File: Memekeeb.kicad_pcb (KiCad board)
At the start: 2 copper layers, 117 parts, among them K1 KEYSW, K10 KEYSW, K11 KEYSW, K12 KEYSW, K14 KEYSW, K15 KEYSW, K16 KEYSW, K17 KEYSW, K18 KEYSW, K19 KEYSW, K2 KEYSW, K20 KEYSW, K21 KEYSW, K22 KEYSW, K23 KEYSW, K24 KEYSW, K25 KEYSW, K27 KEYSW, K28 KEYSW, K29 KEYSW, K3 KEYSW, K30 KEYSW, K31 KEYSW, K32 KEYSW, K33 KEYSW, K34 KEYSW, K35 KEYSW, K36 KEYSW, K37 KEYSW, K38 KEYSW, K4 KEYSW, K40 KEYSW, K41 KEYSW, K42 KEYSW, K43 KEYSW, K44 KEYSW, K45 KEYSW, K46 KEYSW, K47 KEYSW, K48 KEYSW, K49 KEYSW, K5 KEYSW, K50 KEYSW, K51 KEYSW, K6 KEYSW, K7 KEYSW, K8 KEYSW, K9 KEYSW, M2.6_1 VAL**, M2.6_2 VAL**, M2.6_3 VAL**, M2.6_4 VAL**, M2.6_5 VAL**, M2.6_6 VAL**, M2.6_7 VAL**

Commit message: Add unfinished pcb
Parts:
- removed    : LOGO, Graphics:Open-soos
- removed D26, D38, D39, D40, D41, D42, D43, D44, D45, D46, D47, D48, D49, D50, D51, D_ISOENTER1: D, keyboard_parts:D_SOD123_axial
- removed HOLE_M2.6_10, HOLE_M2.6_8, HOLE_M2.6_9, M2.6_1, M2.6_2, M2.6_3, M2.6_4, M2.6_5, M2.6_6, M2.6_7: VAL**, keyboard_parts:HOLE_M2.6
- removed K38, K40, K41, K42, K43, K44, K46, K47, K48, K49, K50, K51: KEYSW, Button_Switch_Keyboard:SW_Cherry_MX1A_1.00u_PCB
- removed K45: KEYSW, Button_Switch_Keyboard:SW_Cherry_MX1A_2.00u_PCB
- removed K_ENTER1, K_RSHFT1: KEYSW, Button_Switch_Keyboard:SW_Cherry_MX1A_1.50u_PCB
- added D_1.25u1: D, keyboard_parts:D_SOD123_axial, F.Cu at (169.1, 71.0)
- added D_2Uspc1: D, keyboard_parts:D_SOD123_axial, F.Cu at (169.1, 68.4)
- added K_1.25u1: KEYSW, Button_Switch_Keyboard:SW_Cherry_MX1A_1.25u_PCB, F.Cu at (148.0, 84.6)
- added K_2Uspc1: KEYSW, Keebio-Parts:MX-Alps-Choc-2U, F.Cu at (123.9, 109.8)
- added K_ENC1: Encoder_switch, Keebio-Parts:RotaryEncoder_Alps_EC11E-Switch_Vertical_H20mm, F.Cu at (276.7, 126.6)
- D1, D10, D11, D12, D13, D14, D15, D16, D17, D18, D19, D2, D20, D21, D22, D23, D24, D25, D27, D28, D29, D3, D30, D31, D32, D33, D34, D35, D36, D37, D4, D5, D6, D7, D8, D9: moved to F.Cu
- K1, K14, K27: footprint Button_Switch_Keyboard:SW_Cherry_MX1A_1.50u_PCB -> Keebio-Parts:MX-Alps-Choc-1U
- K10, K11, K12, K15, K16, K17, K18, K19, K2, K20, K21, K22, K23, K24, K25, K28, K29, K3, K30, K31, K32, K33, K34, K35, K36, K37, K4, K5, K6, K7, K8, K9: footprint Button_Switch_Keyboard:SW_Cherry_MX1A_1.00u_PCB -> Keebio-Parts:MX-Alps-Choc-1U
- K_BCKSPC1: footprint Button_Switch_Keyboard:SW_Cherry_MX1A_1.50u_PCB -> Keebio-Parts:MX_PCB_150H
- SW_RST1: value SW_RST -> SW_PUSH; moved to F.Cu
- moved K_BCKSPC1 220.2 mm to (119.0, 129.5)
- moved K_ISOENTER1 207.6 mm to (124.1, 76.0)
- moved D13 204.0 mm to (137.7, 159.7)
- moved D12 185.2 mm to (137.7, 162.3)
- moved K37 178.1 mm to (114.4, 148.5)
- moved D11 175.9 mm to (128.3, 159.7)
- moved D10 154.4 mm to (137.7, 164.9)
- moved K15 149.1 mm to (263.1, 90.7)
- moved D9 141.4 mm to (137.7, 167.5)
- moved D25 135.1 mm to (166.9, 105.8)
- moved K36 127.3 mm to (142.8, 129.6)
- moved D34 125.9 mm to (109.5, 159.4)
- moved D37 121.6 mm to (169.1, 73.6)
- moved D8 117.2 mm to (147.1, 162.3)
- moved D24 116.4 mm to (166.9, 108.4)
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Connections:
- net Net-(MCU_Pro_Micr0-Pad22) renamed RST
- net Net-(MCU_Pro_Micr0-Pad23) renamed GND
- K_ISOENTER1 pad 2: Net-(D_ISOENTER1-Pad2) -> RowB
- MCU_Pro_Micr0 pad 1: RowA -> Net-(MCU_Pro_Micr0-Pad1)
- MCU_Pro_Micr0 pad 10: ColD -> ColC
- MCU_Pro_Micr0 pad 11: ColE -> ColD
- MCU_Pro_Micr0 pad 12: ColF -> ColE
- MCU_Pro_Micr0 pad 13: Net-(MCU_Pro_Micr0-Pad13) -> ColM
- MCU_Pro_Micr0 pad 14: ColM -> ColL
- MCU_Pro_Micr0 pad 15: ColL -> ColK
- MCU_Pro_Micr0 pad 16: ColK -> ColJ
- MCU_Pro_Micr0 pad 17: ColJ -> ColI
- MCU_Pro_Micr0 pad 18: ColI -> ColH
- MCU_Pro_Micr0 pad 19: ColH -> ColG
- MCU_Pro_Micr0 pad 2: RowB -> Net-(MCU_Pro_Micr0-Pad2)
- MCU_Pro_Micr0 pad 20: ColG -> ColF
- MCU_Pro_Micr0 pad 5: RowC -> RowA
- MCU_Pro_Micr0 pad 6: RowD -> RowB
- MCU_Pro_Micr0 pad 7: ColA -> RowC
- MCU_Pro_Micr0 pad 8: ColB -> ColA
- MCU_Pro_Micr0 pad 9: ColC -> ColB
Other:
- board text removed: "> u/ergorius"

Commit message: Add WS2812B LED Strip support
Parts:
- removed D_2Uspc1: D, keyboard_parts:D_SOD123_axial
- added D_ISOENTR1: D, keyboard_parts:D_SOD123_axial, B.Cu at (283.8, 89.2)
- added LED_DATA1: 0, Keebio-Parts:SinglePad, B.Cu at (89.3, 95.3)
- added LED_GND1: 0, Keebio-Parts:SinglePad, B.Cu at (89.3, 98.6)
- added LED_PWR1: 0, Keebio-Parts:SinglePad, B.Cu at (89.5, 91.9)
- D1, D10, D11, D12, D13, D14, D15, D16, D17, D18, D19, D2, D20, D21, D22, D23, D24, D25, D27, D28, D29, D3, D30, D31, D32, D33, D34, D35, D36, D37, D4, D5, D6, D7, D8, D9, D_1.25u1, SW_RST1: moved to B.Cu
- K1, K10, K11, K12, K14, K15, K16, K17, K18, K19, K2, K20, K21, K22, K23, K24, K25, K27, K28, K29, K3, K30, K31, K32, K33, K34, K35, K36, K37, K4, K5, K6, K7, K8, K9: footprint Keebio-Parts:MX-Alps-Choc-1U -> Keebio-Parts:MX-Alps-Choc-1U-NoLED
- K_1.25u1: footprint Button_Switch_Keyboard:SW_Cherry_MX1A_1.25u_PCB -> Keebio-Parts:MX-Alps-Choc-1U-NoLED
- K_BCKSPC1: footprint Keebio-Parts:MX_PCB_150H -> Keebio-Parts:MX-Alps-Choc-1U-NoLED
- K_ISOENTER1: footprint Button_Switch_Keyboard:SW_Cherry_MX1A_ISOEnter_Plate -> Keebio-Parts:MX-Alps-Choc-2U
- moved K_ENC1 223.0 mm to (61.9, 66.7), turned to 90 degrees
- moved K_BCKSPC1 187.1 mm to (295.3, 66.7)
- moved K15 182.2 mm to (81.0, 85.7)
- moved D13 179.1 mm to (295.6, 75.2)
- moved K_ISOENTER1 174.7 mm to (297.7, 95.2), turned to 270 degrees
- moved D12 159.6 mm to (271.5, 75.3)
- moved D11 150.3 mm to (252.6, 75.2)
- moved K2 145.7 mm to (81.0, 66.7)
- moved K37 144.8 mm to (252.4, 104.8)
- moved K16 140.9 mm to (100.0, 85.7)
- moved K1 134.7 mm to (61.9, 66.7)
- moved D10 131.2 mm to (233.4, 75.2)
- moved K29 129.0 mm to (100.0, 104.8)
- moved K_1.25u1 127.5 mm to (273.9, 104.8)
- moved K4 124.9 mm to (119.1, 66.7)
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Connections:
- D11 pad 1: RowA -> RowD
- D12 pad 1: RowA -> RowD
- D13 pad 1: RowA -> RowD
- D24 pad 1: RowB -> RowD
- D25 pad 1: RowB -> RowD
- D37 pad 1: RowC -> RowD
- D_1.25u1 pad 1: RowC -> RowD
- K11 pad 1: ColK -> ColA
- K12 pad 1: ColL -> ColB
- K24 pad 1: ColK -> ColD
- K25 pad 1: ColL -> ColE
- K37 pad 1: ColK -> ColG
- K_1.25u1 pad 1: ColL -> ColH
- K_2Uspc1 pad 2: Net-(D_2Uspc1-Pad2) -> Net-(D32-Pad2)
- K_BCKSPC1 pad 1: ColM -> ColC
- K_ISOENTER1 pad 1: ColM -> ColF
- K_ISOENTER1 pad 2: RowB -> Net-(D_ISOENTR1-Pad2)
- MCU_Pro_Micr0 pad 1: Net-(MCU_Pro_Micr0-Pad1) -> EncA
- MCU_Pro_Micr0 pad 10: ColC -> RowD
- MCU_Pro_Micr0 pad 11: ColD -> ColA
- MCU_Pro_Micr0 pad 12: ColE -> ColB
- MCU_Pro_Micr0 pad 13: ColM -> ColJ
- MCU_Pro_Micr0 pad 14: ColL -> ColI
- MCU_Pro_Micr0 pad 15: ColK -> ColH
- MCU_Pro_Micr0 pad 16: ColJ -> ColG
- MCU_Pro_Micr0 pad 17: ColI -> ColF
- MCU_Pro_Micr0 pad 18: ColH -> ColC
- MCU_Pro_Micr0 pad 19: ColG -> ColD
- MCU_Pro_Micr0 pad 2: Net-(MCU_Pro_Micr0-Pad2) -> EncB
- MCU_Pro_Micr0 pad 20: ColF -> ColE
- MCU_Pro_Micr0 pad 21: Net-(MCU_Pro_Micr0-Pad21) -> RGB_PWR
- MCU_Pro_Micr0 pad 5: RowA -> RGB
- MCU_Pro_Micr0 pad 6: RowB -> Net-(MCU_Pro_Micr0-Pad6)
- MCU_Pro_Micr0 pad 7: RowC -> RowA
- MCU_Pro_Micr0 pad 8: ColA -> RowB
- MCU_Pro_Micr0 pad 9: ColB -> RowC

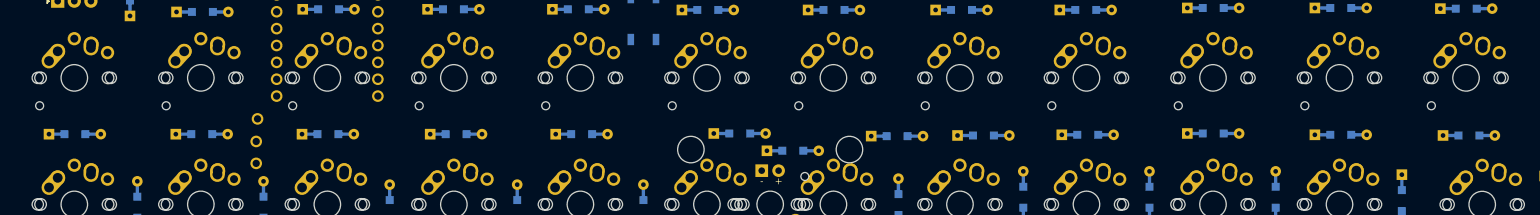
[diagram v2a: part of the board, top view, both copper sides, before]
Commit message: Move WS2812 pins to the side, rearrange diode footprints
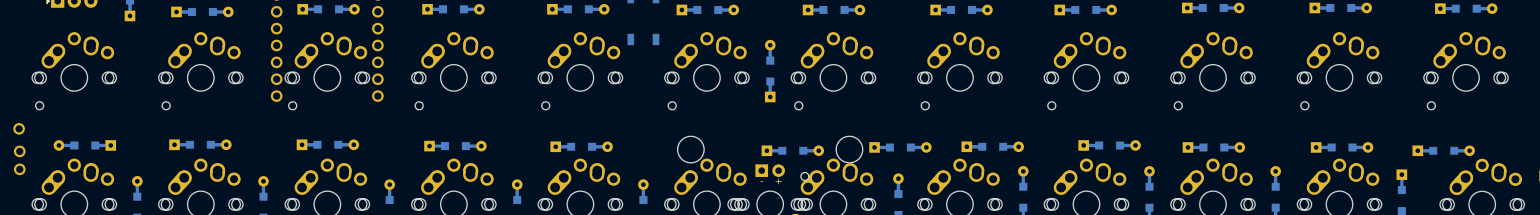
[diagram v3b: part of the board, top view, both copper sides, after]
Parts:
- LED_DATA1: value 0 -> DATA
- LED_GND1: value 0 -> GND
- LED_PWR1: value 0 -> PWR
- moved LED_PWR1 35.9 mm to (53.6, 93.4)
- moved LED_DATA1 35.6 mm to (53.7, 96.8)
- moved LED_GND1 35.6 mm to (53.7, 99.5)
- moved D19 10.5 mm to (166.7, 84.7), turned to 90 degrees
- moved D25 4.44 mm to (268.1, 96.7)
- moved D22 3.67 mm to (217.8, 95.9)
- moved D14 2.27 mm to (63.5, 95.9), turned to 180 degrees
- moved D21 2.20 mm to (200.2, 96.1)
- moved D23 2.10 mm to (233.5, 96.2)
- moved D24 1.91 mm to (252.8, 96.2)
- moved D18 1.90 mm to (138.3, 96.1)
- moved D17 1.80 mm to (119.3, 96.0)
- moved D20 1.77 mm to (186.3, 96.2)
- moved D15 1.61 mm to (80.9, 95.8)
- moved D16 1.60 mm to (100.1, 95.8)
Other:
- board text added: "WS2812"
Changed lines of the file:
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@@
   (general
     (thickness 1.6)
-    (drawings 0)
+    (drawings 1)
     (tracks 0)
     (zones 0)
@@
   )
   (module keyboard_parts:D_SOD123_axial (layer B.Cu)
-    (at 62 94.2)
+    (at 63.5 95.9 180)
     (attr smd)
-    (fp_text reference D14 (at 0 -1.925) (layer B.SilkS)
+    (fp_text reference D14 (at 0 -1.925 180) (layer B.SilkS)
       (effects (font (size 0.8 0.8) (thickness 0.15)) (justify mirror))
     )
-    (fp_text value D (at 0 1.925) (layer B.SilkS) hide
+    (fp_text value D (at 0 1.925 180) (layer B.SilkS) hide
       (effects (font (size 0.8 0.8) (thickness 0.15)) (justify mirror))
     )
@@
     (fp_line (start 2.8 1.2) (end 2.8 -1.2) (layer B.SilkS) (width 0.2))
     (fp_line (start 2.8 -1.2) (end -3 -1.2) (layer B.SilkS) (width 0.2))
-    (pad 2 smd rect (at 1.575 0) (size 1.2 1.2) (layers B.Cu B.Paste B.Mask)
+    (pad 2 smd rect (at 1.575 0 180) (size 1.2 1.2) (layers B.Cu B.Paste B.Mask)
       (net 14 "Net-(D14-Pad2)"))
-    (pad 1 smd rect (at -1.575 0) (size 1.2 1.2) (layers B.Cu B.Paste B.Mask)
+    (pad 1 smd rect (at -1.575 0 180) (size 1.2 1.2) (layers B.Cu B.Paste B.Mask)
       (net 38 RowB))
-    (pad 1 thru_hole rect (at -3.9 0) (size 1.6 1.6) (drill 0.7) (layers *.Cu *.Mask B.SilkS)
+    (pad 1 thru_hole rect (at -3.9 0 180) (size 1.6 1.6) (drill 0.7) (layers *.Cu *.Mask B.SilkS)
       (net 38 RowB))
-    (pad 2 thru_hole circle (at 3.9 0) (size 1.6 1.6) (drill 0.7) (layers *.Cu *.Mask B.SilkS)
+    (pad 2 thru_hole circle (at 3.9 0 180) (size 1.6 1.6) (drill 0.7) (layers *.Cu *.Mask B.SilkS)
       (net 14 "Net-(D14-Pad2)"))
-    (pad 1 smd rect (at -2.7 0) (size 2.5 0.5) (layers B.Cu)
+    (pad 1 smd rect (at -2.7 0 180) (size 2.5 0.5) (layers B.Cu)
       (net 38 RowB) (solder_mask_margin -999))
-    (pad 2 smd rect (at 2.7 0) (size 2.5 0.5) (layers B.Cu)
+    (pad 2 smd rect (at 2.7 0 180) (size 2.5 0.5) (layers B.Cu)
       (net 14 "Net-(D14-Pad2)") (solder_mask_margin -999))
   )
   (module keyboard_parts:D_SOD123_axial (layer B.Cu)
-    (at 81.1 94.2)
+    (at 80.9 95.8)
     (attr smd)
     (fp_text reference D15 (at 0 -1.925) (layer B.SilkS)
@@
   )
   (module keyboard_parts:D_SOD123_axial (layer B.Cu)
-    (at 100.1 94.2)
+    (at 100.1 95.8)
     (attr smd)
     (fp_text reference D16 (at 0 -1.925) (layer B.SilkS)
@@
   )
   (module keyboard_parts:D_SOD123_axial (layer B.Cu)
-    (at 119.4 94.2)
+    (at 119.3 96)
     (attr smd)
     (fp_text reference D17 (at 0 -1.925) (layer B.SilkS)
@@
   )
   (module keyboard_parts:D_SOD123_axial (layer B.Cu)
-    (at 138.3 94.2)
+    (at 138.3 96.1)
     (attr smd)
     (fp_text reference D18 (at 0 -1.925) (layer B.SilkS)
@@
   )
   (module keyboard_parts:D_SOD123_axial (layer B.Cu)
-    (at 162.1 94.1)
+    (at 166.7 84.7 90)
     (attr smd)
-    (fp_text reference D19 (at 0 -1.925) (layer B.SilkS)
+    (fp_text reference D19 (at 0 -1.925 90) (layer B.SilkS)
       (effects (font (size 0.8 0.8) (thickness 0.15)) (justify mirror))
     )
-    (fp_text value D (at 0 1.925) (layer B.SilkS) hide
+    (fp_text value D (at 0 1.925 90) (layer B.SilkS) hide
       (effects (font (size 0.8 0.8) (thickness 0.15)) (justify mirror))
     )
@@
     (fp_line (start 2.8 1.2) (end 2.8 -1.2) (layer B.SilkS) (width 0.2))
     (fp_line (start 2.8 -1.2) (end -3 -1.2) (layer B.SilkS) (width 0.2))
-    (pad 2 smd rect (at 1.575 0) (size 1.2 1.2) (layers B.Cu B.Paste B.Mask)
+    (pad 2 smd rect (at 1.575 0 90) (size 1.2 1.2) (layers B.Cu B.Paste B.Mask)
       (net 19 "Net-(D19-Pad2)"))
-    (pad 1 smd rect (at -1.575 0) (size 1.2 1.2) (layers B.Cu B.Paste B.Mask)
+    (pad 1 smd rect (at -1.575 0 90) (size 1.2 1.2) (layers B.Cu B.Paste B.Mask)
       (net 38 RowB))
-    (pad 1 thru_hole rect (at -3.9 0) (size 1.6 1.6) (drill 0.7) (layers *.Cu *.Mask B.SilkS)
+    (pad 1 thru_hole rect (at -3.9 0 90) (size 1.6 1.6) (drill 0.7) (layers *.Cu *.Mask B.SilkS)
       (net 38 RowB))
-    (pad 2 thru_hole circle (at 3.9 0) (size 1.6 1.6) (drill 0.7) (layers *.Cu *.Mask B.SilkS)
+    (pad 2 thru_hole circle (at 3.9 0 90) (size 1.6 1.6) (drill 0.7) (layers *.Cu *.Mask B.SilkS)
       (net 19 "Net-(D19-Pad2)"))
-    (pad 1 smd rect (at -2.7 0) (size 2.5 0.5) (layers B.Cu)
+    (pad 1 smd rect (at -2.7 0 90) (size 2.5 0.5) (layers B.Cu)
       (net 38 RowB) (solder_mask_margin -999))
-    (pad 2 smd rect (at 2.7 0) (size 2.5 0.5) (layers B.Cu)
+    (pad 2 smd rect (at 2.7 0 90) (size 2.5 0.5) (layers B.Cu)
       (net 19 "Net-(D19-Pad2)") (solder_mask_margin -999))
   )
   (module keyboard_parts:D_SOD123_axial (layer B.Cu)
-    (at 185.8 94.5)
+    (at 186.3 96.2)
     (attr smd)
     (fp_text reference D20 (at 0 -1.925) (layer B.SilkS)
@@
   )
   (module keyboard_parts:D_SOD123_axial (layer B.Cu)
-    (at 198.8 94.4)
+    (at 200.2 96.1)
     (attr smd)
     (fp_text reference D21 (at 0 -1.925) (layer B.SilkS)
@@
   )
   (module keyboard_parts:D_SOD123_axial (layer B.Cu)
-    (at 214.5 94.3)
+    (at 217.8 95.9)
     (attr smd)
     (fp_text reference D22 (at 0 -1.925) (layer B.SilkS)
@@
   )
   (module keyboard_parts:D_SOD123_axial (layer B.Cu)
-    (at 233.4 94.1)
+    (at 233.5 96.2)
     (attr smd)
     (fp_text reference D23 (at 0 -1.925) (layer B.SilkS)
@@
   )
   (module keyboard_parts:D_SOD123_axial (layer B.Cu)
-    (at 252.6 94.3)
+    (at 252.8 96.2)
     (attr smd)
     (fp_text reference D24 (at 0 -1.925) (layer B.SilkS)
@@
   )
   (module keyboard_parts:D_SOD123_axial (layer B.Cu)
-    (at 271.9 94.4)
+    (at 268.1 96.7)
     (attr smd)
     (fp_text reference D25 (at 0 -1.925) (layer B.SilkS)
@@
   )
   (module Keebio-Parts:SinglePad (layer B.Cu)
-    (at 89.3 95.3)
+    (at 53.7 96.8)
     (fp_text reference LED_DATA1 (at 0 1.778) (layer Dwgs.User) hide
       (effects (font (size 1 1) (thickness 0.2)))
     )
-    (fp_text value 0 (at 0 -1.778) (layer B.SilkS)
+    (fp_text value DATA (at 0 -1.778) (layer B.SilkS)
       (effects (font (size 1 1) (thickness 0.2)) (justify mirror))
     )
@@
   )
   (module Keebio-Parts:SinglePad (layer B.Cu)
-    (at 89.3 98.6)
+    (at 53.7 99.5)
     (fp_text reference LED_GND1 (at 0 1.778) (layer Dwgs.User) hide
       (effects (font (size 1 1) (thickness 0.2)))
     )
-    (fp_text value 0 (at 0 -1.778) (layer B.SilkS)
+    (fp_text value GND (at 0 -1.778) (layer B.SilkS)
       (effects (font (size 1 1) (thickness 0.2)) (justify mirror))
     )
@@
   )
   (module Keebio-Parts:SinglePad (layer B.Cu)
-    (at 89.5 91.9)
+    (at 53.6 93.4)
     (fp_text reference LED_PWR1 (at 0 1.778) (layer Dwgs.User) hide
       (effects (font (size 1 1) (thickness 0.2)))
     )
-    (fp_text value 0 (at 0 -1.778) (layer B.SilkS)
+    (fp_text value PWR (at 0 -1.778) (layer B.SilkS)
       (effects (font (size 1 1) (thickness 0.2)) (justify mirror))
     )
@@
       (net 62 RGB_PWR))
   )
+  (gr_text WS2812 (at 56.1 95.9 270) (layer B.SilkS)
+    (effects (font (size 1.2 1.2) (thickness 0.3)) (justify mirror))
+  )
 )
